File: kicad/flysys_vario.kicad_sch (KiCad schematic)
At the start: 51 parts, among them J1 S2B-PH-SM4-TB, J2 Debug pads 1x6, Q1 AO3400A, Q2 AO3400A, SW1 KMR211NG LFS, U1 BQ24075RGTR, U2 BMI323, U3 TLV75533PDBVR, U4 ESP32-S3-MINI-1-N8, U5 BMP581

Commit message: Add hard-off power path and bootloader buttons
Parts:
- removed J2: Debug pads 1x6, Local_DebugPads:DebugPads_1x06_1.27mm, symbol FlySys:DebugPads_1x06_1.27mm
- added D2, D3, D4: 1N4148W, Diodes_Inc_1N4148W:1N4148W, symbol FlySys:1N4148W
- added Q3, Q5: AO3400A, Alpha_Omega_AO3400A:AO3400A, symbol FlySys:AO3400A
- added Q4: DMP3098L, Diodes_Inc_DMP3098L:DMP3098L, symbol FlySys:DMP3098L
- added R23, R26, R28: 1M, UNI_ROYAL_0603WAF1004T5E:R0603, symbol FlySys:R
- added R24: 100k, UNI_ROYAL_0603WAF1003T5E:R0603, symbol FlySys:R
- added R25: 100R, UNI_ROYAL_0603WAF1000T5E:R0603, symbol FlySys:R
- added R27: 4.7k, UNI_ROYAL_0603WAF4701T5E:R0603, symbol FlySys:R
- added SW2, SW3: KMR211NG LFS, CK_KMR211NG_LFS:KMR211NG_LFS, symbol FlySys:KMR211NG_LFS
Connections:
- net +3V3: now also R24.2, R27.2
- net BAT: now also Q4.3 (D), R23.2; no longer J1.1 (BAT+)
- net BOOT_USER_BTN_N: now also SW2.1 (A), SW2.2 (A); no longer SW1.1 (A), SW1.2 (A)
- net EN: now also SW3.1 (A), SW3.2 (A)
- net GND: now also Q3.2 (S), Q5.2 (S), R26.2, SW2.3 (B), SW2.4 (B), SW3.3 (B), SW3.4 (B); no longer U1.15 (SYSOFF)
- net PWR_BTN_N: now reaches U4.11 (IO7)
- net PWR_BTN_N: now also D2.2 (A), R27.1
- net PWR_HOLD: now reaches U4.14 (IO10)
- net PWR_HOLD: now also R25.1
- net RXD0: no longer names the net of U4.40 (RXD0)
- net TXD0: no longer names the net of U4.39 (TXD0)
- new net BAT_RAW: J1.1 (BAT+), Q4.2 (S), R28.2
- new net BAT_SWITCH_GATE: D3.2 (A), Q4.1 (G), Q5.3 (D), R28.1
- new net CHG_SYSOFF: D4.2 (A), Q3.3 (D), R23.1, U1.15 (SYSOFF)
- new net PWR_HOLD_GATE: Q3.1 (G), Q5.1 (G), R24.1, R25.2, R26.1
- new net PWR_SW_N: D2.1 (K), D3.1 (K), D4.1 (K), SW1.1 (A), SW1.2 (A)

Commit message: Boot, reset, USB protection
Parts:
- D1: value USBLC6-2SC6 -> USBLC6-2SC6Y; symbol FlySys:USBLC6-2SC6 -> FlySys:USBLC6-2SC6Y; DigiKey Part Number 497-5235-1-ND -> 497-11882-1-ND; DigiKey URL https://www.digikey.com/en/products/detail/stmicroelectronics/USBLC6-2SC6/1040559 -> https://www.digikey.com/en/products/detail/stmicroelectronics/USBLC6-2SC6Y/2819177; MPN USBLC6-2SC6 -> USBLC6-2SC6Y
- SW2: footprint CK_KMR211NG_LFS:KMR211NG_LFS -> CK_KMR211NG_LFS:KMR211NG_LFS_BOOT
- SW3: footprint CK_KMR211NG_LFS:KMR211NG_LFS -> CK_KMR211NG_LFS:KMR211NG_LFS_RST
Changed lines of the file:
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@@
 	)
 	(symbol
-		(lib_id "FlySys:USBLC6-2SC6")
+		(lib_id "FlySys:USBLC6-2SC6Y")
 		(at 144.78 74.93 0)
 		(unit 1)
@@
 			)
 		)
-		(property "Value" "USBLC6-2SC6"
+		(property "Value" "USBLC6-2SC6Y"
 			(at 144.78 87.55 0)
 			(effects
@@
 			)
 		)
-		(property "Description" "USB ESD protection diode array"
+		(property "Description" "Automotive USB ESD protection diode array, SOT-23-6"
 			(at 144.78 74.93 0)
 			(effects
@@
 			)
 		)
-		(property "MPN" "USBLC6-2SC6"
+		(property "MPN" "USBLC6-2SC6Y"
 			(at 144.78 74.93 0)
 			(effects
@@
 			)
 		)
-		(property "DigiKey Part Number" "497-5235-1-ND"
+		(property "DigiKey Part Number" "497-11882-1-ND"
 			(at 144.78 74.93 0)
 			(effects
@@
 			)
 		)
-		(property "DigiKey URL" "https://www.digikey.com/en/products/detail/stmicroelectronics/USBLC6-2SC6/1040559"
+		(property "DigiKey URL" "https://www.digikey.com/en/products/detail/stmicroelectronics/USBLC6-2SC6Y/2819177"
 			(at 144.78 74.93 0)
 			(effects
@@
 			)
 		)
-		(property "Footprint" "CK_KMR211NG_LFS:KMR211NG_LFS"
+		(property "Footprint" "CK_KMR211NG_LFS:KMR211NG_LFS_BOOT"
 			(at 430.53 88.01 0)
 			(effects
@@
 			)
 		)
-		(property "Footprint" "CK_KMR211NG_LFS:KMR211NG_LFS"
+		(property "Footprint" "CK_KMR211NG_LFS:KMR211NG_LFS_RST"
 			(at 430.53 115.95 0)
 			(effects

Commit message: Point to digikey.si
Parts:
- BZ1: DigiKey URL https://www.digikey.com/en/products/detail/same-sky-formerl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 -> https://www.digikey.si/en/products/detail/same-sky-formerly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
- C1, C13, C14, C3, C7, C8, C9: DigiKey URL https://www.digikey.com/en/products/detail/samsung-electro-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 -> https://www.digikey.si/en/products/detail/samsung-electro-m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
- C10, C11, C12, C2, C4, C5, C6: DigiKey URL https://www.digikey.com/en/products/detail/yageo/CC0603KRX7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 -> https://www.digikey.si/en/products/detail/yageo/CC0603KRX7R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
- D1: DigiKey URL https://www.digikey.com/en/products/detail/stmicroelectroni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 -> https://www.digikey.si/en/products/detail/stmicroelectronic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
- D2, D3, D4, Q4: DigiKey URL https://www.digikey.com/en/products/detail/diodes-incorpora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 -> https://www.digikey.si/en/products/detail/diodes-incorporat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
- J1: DigiKey URL https://www.digikey.com/en/products/detail/jst-sales-americ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 -> https://www.digikey.si/en/products/detail/jst-sales-america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
- LED1, LED2: DigiKey URL https://www.digikey.com/en/products/detail/lite-on-inc/LTST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 -> https://www.digikey.si/en/products/detail/lite-on-inc/LTST-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
- Q1, Q2, Q3, Q5: DigiKey URL https://www.digikey.com/en/products/detail/alpha-omega-semi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 -> https://www.digikey.si/en/products/detail/alpha-omega-semic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
- R1, R10, R11, R12, R13, R14, R15, R16, R17, R18, R19, R2, R20, R21, R22, R23, R24, R25, R26, R27, R28, R3, R4, R5, R6, R7, R8, R9: DigiKey URL https://www.digikey.com/en/products/detail/yageo/RC0603FR-0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 -> https://www.digikey.si/en/products/detail/yageo/RC0603FR-07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
- SW1, SW2, SW3: DigiKey URL https://www.digikey.com/en/products/detail/c-k/KMR211NG-LFS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 -> https://www.digikey.si/en/products/detail/c-k/KMR211NG-LFS/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
- U1, U3: DigiKey URL https://www.digikey.com/en/products/detail/texas-instrument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 -> https://www.digikey.si/en/products/detail/texas-instruments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
- U2, U5: DigiKey URL https://www.digikey.com/en/products/detail/bosch-sensortec/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 -> https://www.digikey.si/en/products/detail/bosch-sensortec/B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
- U4: DigiKey URL https://www.digikey.com/en/products/detail/espressif-system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 -> https://www.digikey.si/en/products/detail/espressif-systems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
- USB1: DigiKey URL https://www.digikey.com/en/products/detail/gct/USB4105-GF-A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 -> https://www.digikey.si/en/products/detail/gct/USB4105-GF-A/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

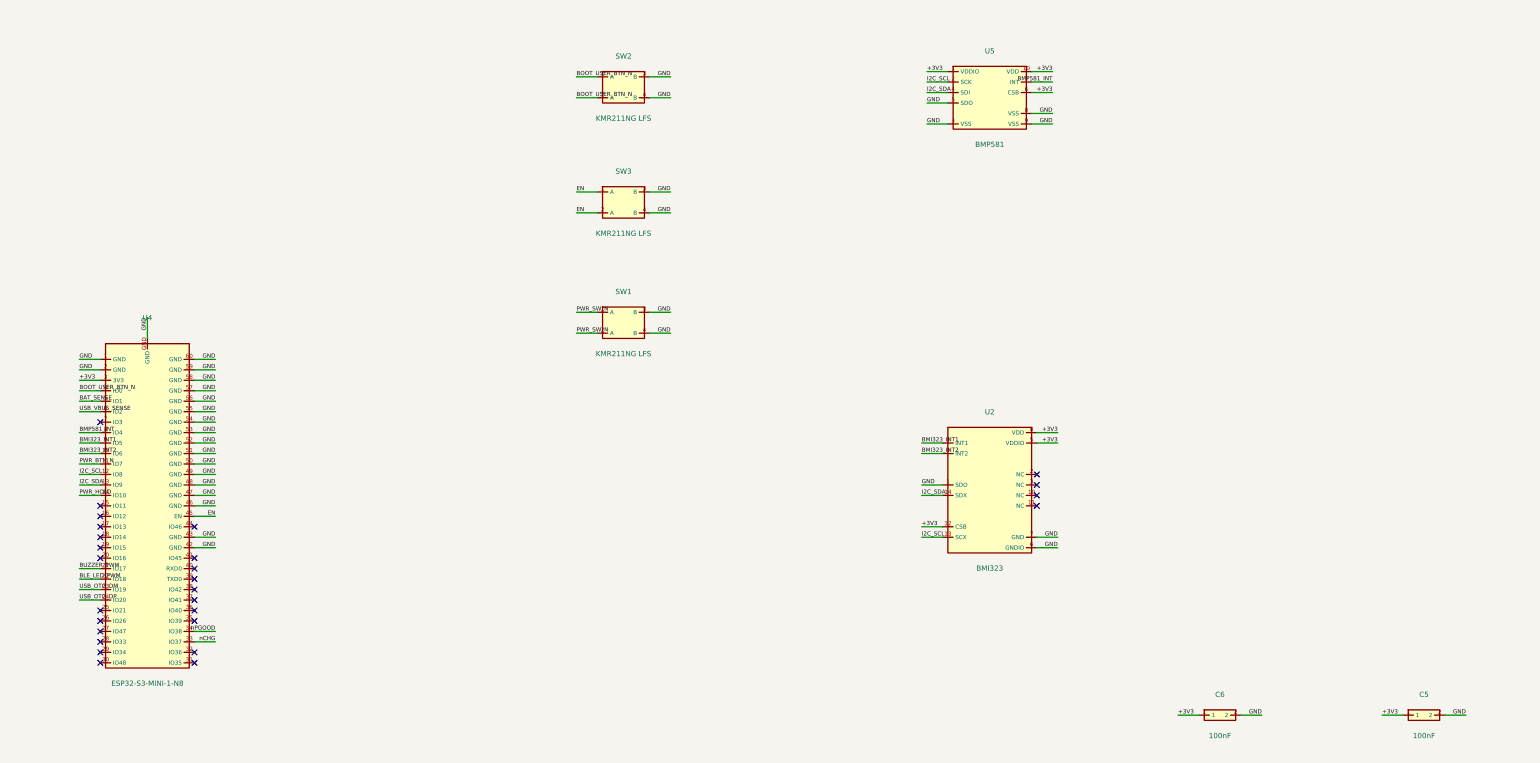
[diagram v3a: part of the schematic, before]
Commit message: Change ESP add antenna
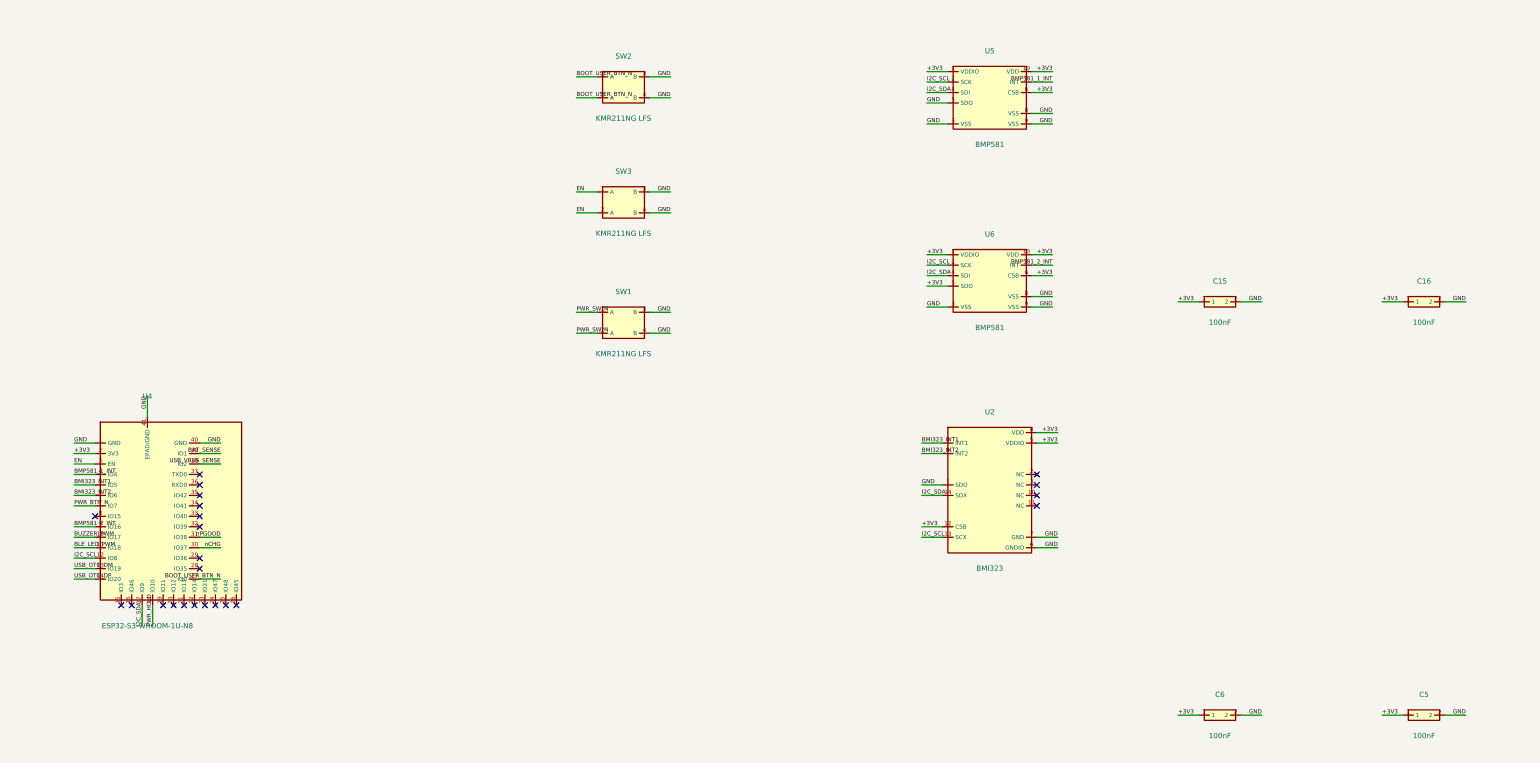
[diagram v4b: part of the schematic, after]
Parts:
- added C15, C16: 100nF, YAGEO_CC0603KRX7R9BB104:C0603, symbol FlySys:C
- added U6: BMP581, Bosch_Sensortec_BMP581:BMP581_LGA10_2x2mm, symbol FlySys:BMP581
- Q4: DigiKey Part Number DMP3098L-7DICT-ND -> DMP3098LDICT-ND; DigiKey URL https://www.digikey.si/en/products/detail/diodes-incorporated/DMP3098L-7/1964698 -> https://www.digikey.si/en/products/detail/diodes-incorporated/DMP3098L-7/1964699
- U4: value ESP32-S3-MINI-1-N8 -> ESP32-S3-WROOM-1U-N8; footprint Espressif_Systems_ESP32_S3_MINI_1_N8:BULETM-SMD_ESP32-S3-MINI-1-N8 -> Espressif_Systems_ESP32_S3_WROOM_1U_N8:ESP32-S3-WROOM-1U-N8; symbol FlySys:ESP32-S3-MINI-1-N8 -> FlySys:ESP32-S3-WROOM-1U-N8; DigiKey Part Number 5407-ESP32-S3-MINI-1-N8CT-ND -> 1965-ESP32-S3-WROOM-1U-N8CT-ND; DigiKey URL https://www.digikey.si/en/products/detail/espressif-systems/ESP32-S3-MINI-1-N8/15295890 -> https://www.digikey.si/en/products/detail/espressif-systems/ESP32-S3-WROOM-1U-N8/16162635; MPN ESP32-S3-MINI-1-N8 -> ESP32-S3-WROOM-1U-N8
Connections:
- net +3V3: now also U4.2 (3V3), C15.1, C16.1, U6.1 (VDDIO), U6.10 (VDD), U6.5 (SDO), U6.6 (CSB); no longer U4.3 (3V3)
- net BAT_SENSE: now also U4.39 (IO1); no longer U4.5 (IO1)
- net BLE_LED_PWM: now also U4.11 (IO18); no longer U4.22 (IO18)
- net BMI323_INT1: now also U4.5 (IO5); no longer U4.9 (IO5)
- net BMI323_INT2: now also U4.6 (IO6); no longer U4.10 (IO6)
- net BOOT_USER_BTN_N: now also U4.27 (IO0); no longer U4.4 (IO0)
- net BUZZER_PWM: now also U4.10 (IO17); no longer U4.21 (IO17)
- net EN: now also U4.3 (EN); no longer U4.45 (EN)
- net GND: now also U4.40 (GND), U4.41 (EPAD/GND), C15.2, C16.2, U6.3 (VSS), U6.8 (VSS), U6.9 (VSS); no longer U4.2 (GND), U4.42 (GND), U4.43 (GND), U4.46 (GND), U4.47 (GND), U4.48 (GND), U4.49 (GND), U4.50 (GND), U4.51 (GND), U4.52 (GND), U4.53 (GND), U4.54 (GND), U4.55 (GND), U4.56 (GND), U4.57 (GND), U4.58 (GND), U4.59 (GND), U4.60 (GND), U4.GND
- net I2C_SCL: now also U6.2 (SCK)
- net I2C_SDA: now also U4.17 (IO9), U6.4 (SDI); no longer U4.13 (IO9)
- net PWR_BTN_N: now also U4.7 (IO7); no longer U4.11 (IO7)
- net PWR_HOLD: now also U4.18 (IO10); no longer U4.14 (IO10)
- net USB_OTG_DM: now also U4.13 (IO19); no longer U4.23 (IO19)
- net USB_OTG_DP: now also U4.14 (IO20); no longer U4.24 (IO20)
- net USB_VBUS_SENSE: now also U4.38 (IO2); no longer U4.6 (IO2)
- net nCHG: now also U4.30 (IO37); no longer U4.33 (IO37)
- net nPGOOD: now also U4.31 (IO38); no longer U4.34 (IO38)
- net BMP581_INT: no longer names the net of U4.8 (IO15)
- net BMP581_INT: no longer U5.7 (INT)
- new net BMP581_1_INT: U4.4 (IO4), U5.7 (INT)
- new net BMP581_2_INT: U4.9 (IO16), U6.7 (INT)
- no-connect marks 30 -> 26
